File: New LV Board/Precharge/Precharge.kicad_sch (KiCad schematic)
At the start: 12 parts, among them J1 Conn_01x07, Q1 DMN3404L, U1 LM324, U2 Optocoupler

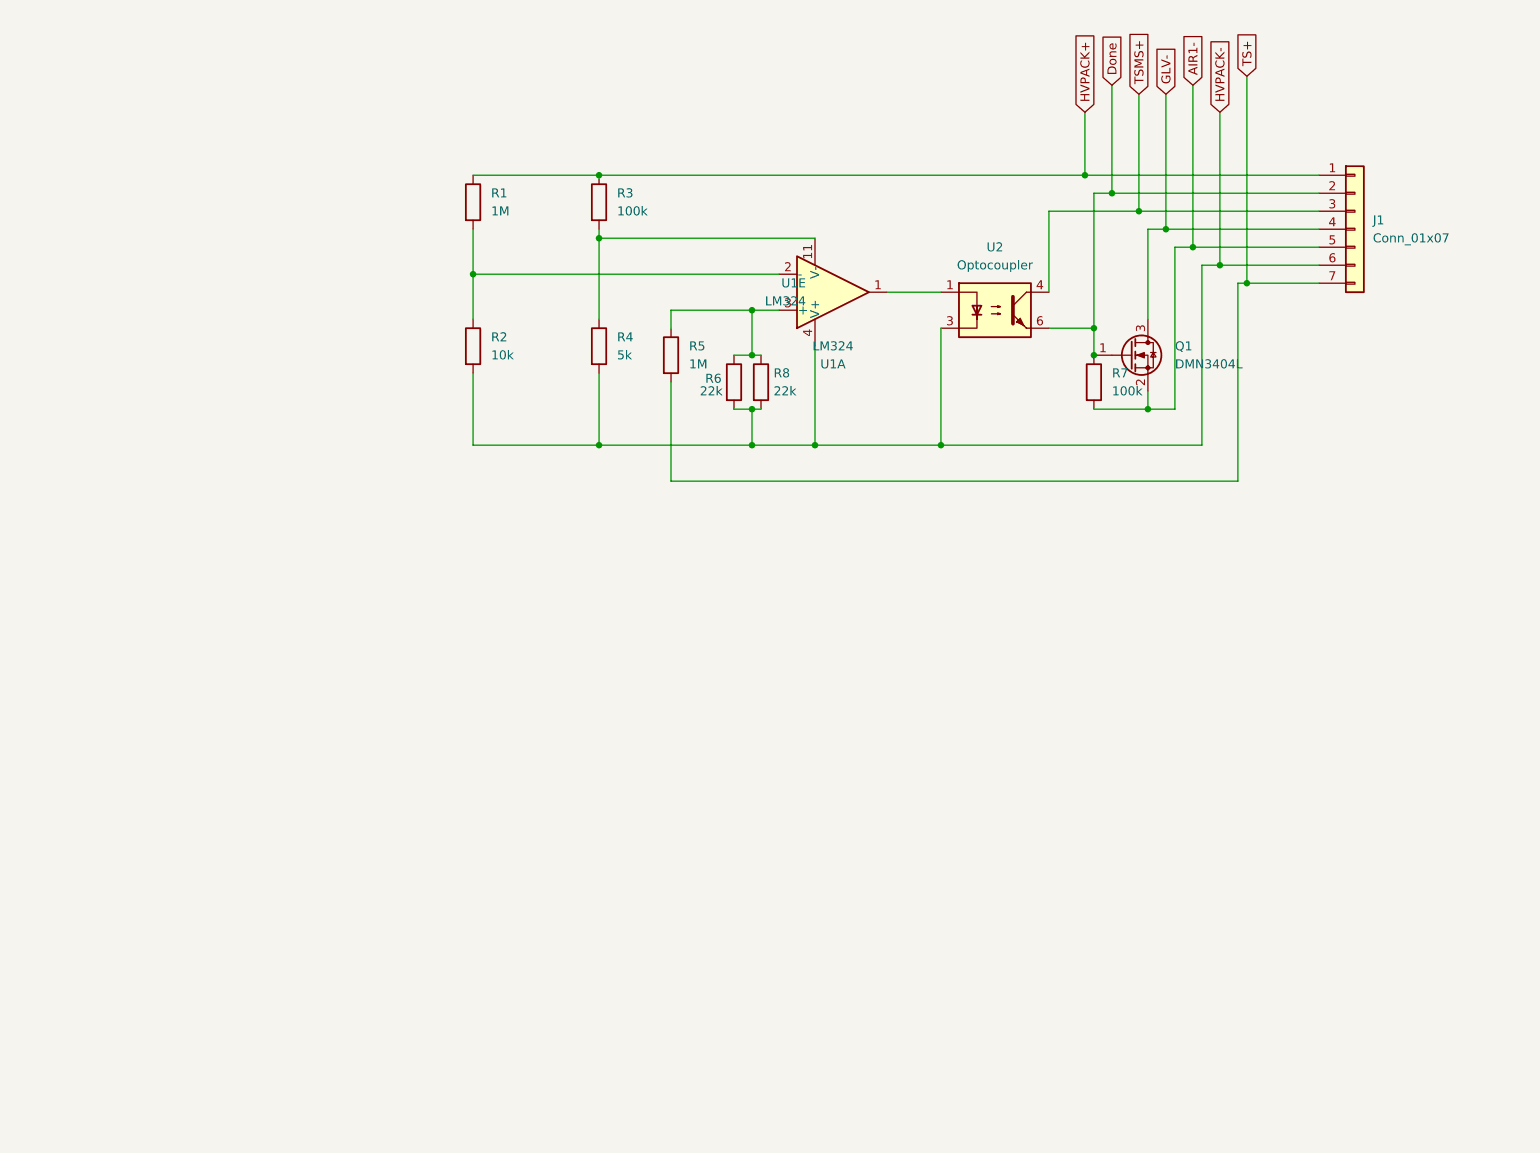
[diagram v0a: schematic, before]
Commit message: Update Precharge.kicad_sch
Added 555 Timer to Precharge design. PMOS Orientation makes it look ugly but it's chill. The 1ms that the pmos for the optocoupler is on will not effect it because during the first ms the opamp output is low.
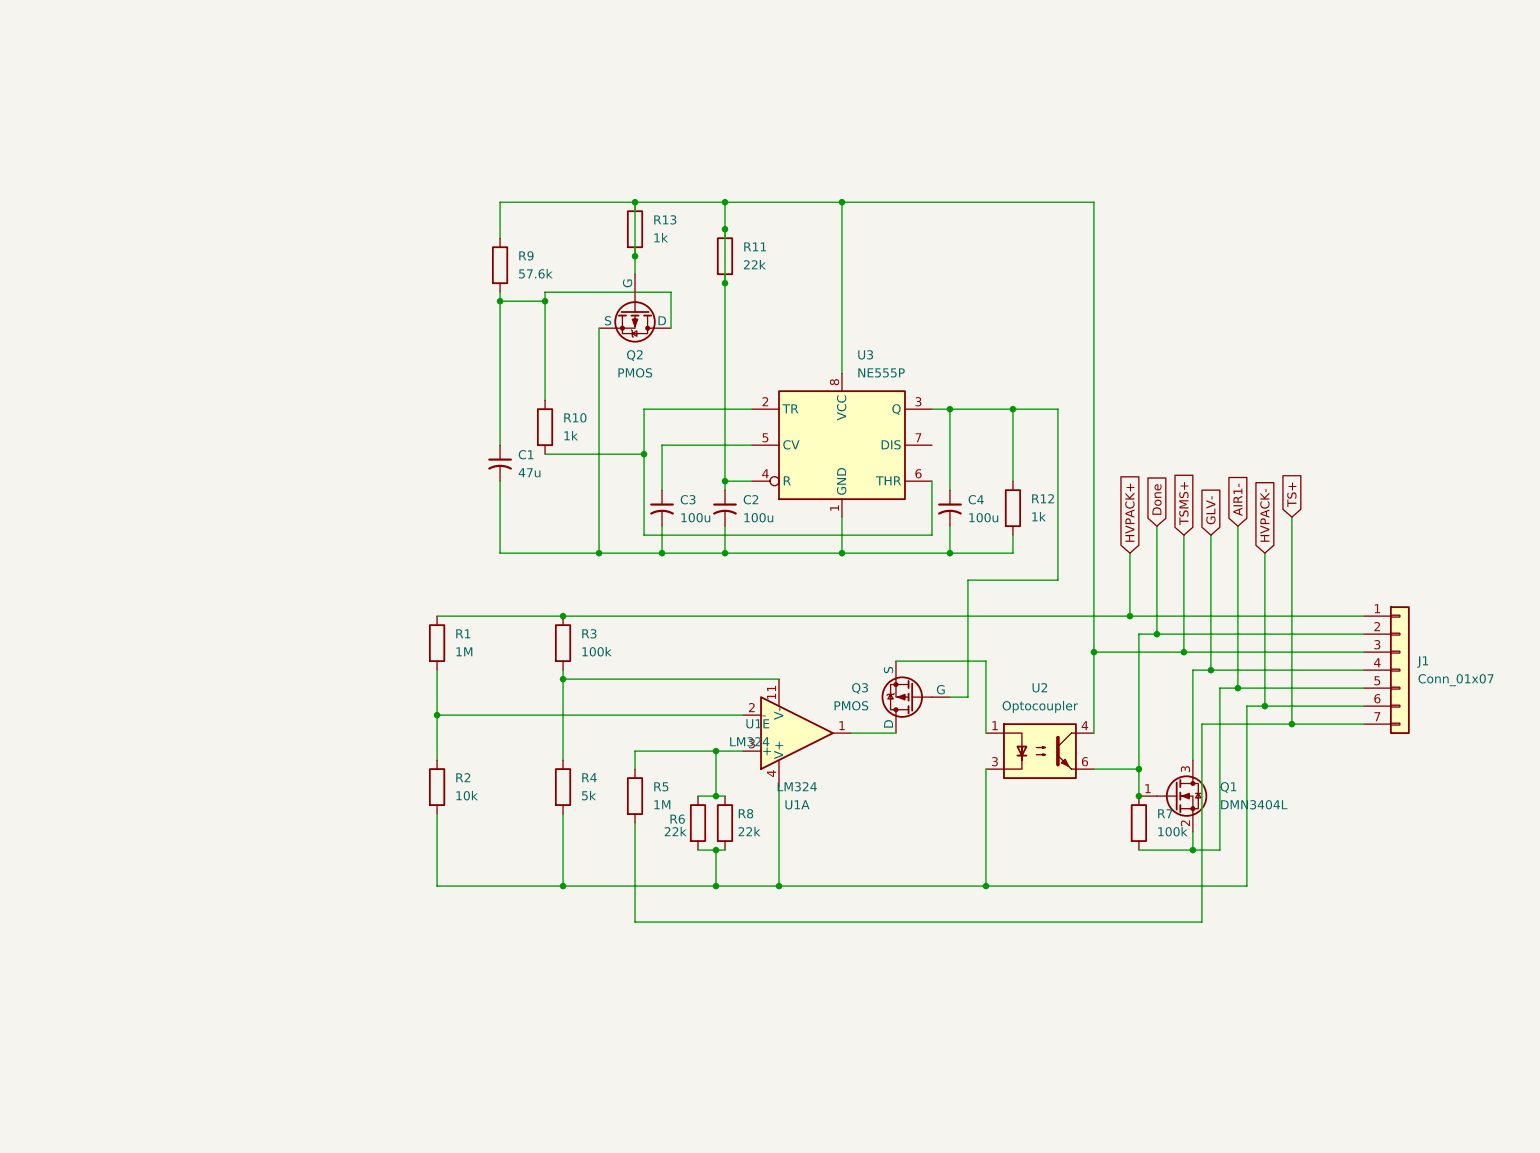
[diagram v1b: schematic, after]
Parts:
- added C1: 47u, symbol Device:C_Small_US
- added C2, C3, C4: 100u, symbol Device:C_Small_US
- added Q2, Q3: PMOS, symbol Simulation_SPICE:PMOS
- added R10, R12, R13: 1k, Resistor_THT:R_Axial_DIN0411_L9.9mm_D3.6mm_P7.62mm_Vertical, symbol Device:R
- added R11: 22k, Resistor_THT:R_Axial_DIN0411_L9.9mm_D3.6mm_P7.62mm_Vertical, symbol Device:R
- added R9: 57.6k, Resistor_THT:R_Axial_DIN0411_L9.9mm_D3.6mm_P7.62mm_Vertical, symbol Device:R
- added U3: NE555P, Package_DIP:DIP-8_W7.62mm, symbol Timer:NE555P
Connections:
- net TSMS+: now also C2.1, Q2.2 (G), R11.1, R11.2, R13.1, R13.2, R9.1, U3.4 (R), U3.8 (VCC)
- net at U1.1: now also Q3.1 (D); no longer U2.1
- new net: C4.1, Q3.2 (G), R12.1, U3.3 (Q)
- new net: Q3.3 (S), U2.1
- new net: C1.1, Q2.1 (D), R10.1, R9.2
- new net: R10.2, U3.2 (TR), U3.6 (THR)
- new net: C1.2, C2.2, C3.2, C4.2, Q2.3 (S), R12.2, U3.1 (GND)
- new net: C3.1, U3.5 (CV)
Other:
- moved on the sheet: J1, Q1, R1, R2, R3, R4, R5, R6, R7, R8, U1A, U1E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

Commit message: Added 555 timer to schematic
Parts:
- removed unit 1 of U1
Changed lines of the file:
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@@
-	)
-	(symbol
-		(lib_id "Amplifier_Operational:LM324")
-		(at 128.27 119.38 0)
-		(mirror x)
-		(unit 1)
-		(exclude_from_sim no)
-		(in_bom yes)
-		(on_board yes)
-		(dnp no)
-		(property "Reference" "U1"
-			(at 128.27 129.54 0)
-			(effects
-				(font
-					(size 1.27 1.27)
-				)
-			)
-		)
-		(property "Value" "LM324"
-			(at 128.27 127 0)
-			(effects
-				(font
-					(size 1.27 1.27)
-				)
-			)
-		)
-		(property "Footprint" "Package_DIP:CERDIP-14_W7.62mm_SideBrazed"
-			(at 127 121.92 0)
-			(effects
-				(font
-					(size 1.27 1.27)
-				)
-				(hide yes)
-			)
-		)
-		(property "Datasheet" "https://www.ti.com/general/docs/suppproductinfo.tsp?distId=10&gotoUrl=http%253A%252F%252Fwww.ti.com%252Flit%252Fgpn%252Flm224"
-			(at 129.54 124.46 0)
-			(effects
-				(font
-					(size 1.27 1.27)
-				)
-				(hide yes)
-			)
-		)
-		(property "Description" "Low-Power, Quad-Operational Amplifiers, DIP-14/SOIC-14/SSOP-14"
-			(at 128.27 119.38 0)
-			(effects
-				(font
-					(size 1.27 1.27)
-				)
-				(hide yes)
-			)
-		)
-		(pin "2"
-		)
-		(pin "3"
-		)
-		(pin "10"
-		)
-		(pin "7"
-		)
-		(pin "6"
-		)
-		(pin "9"
-		)
-		(pin "11"
-		)
-		(pin "14"
-		)
-		(pin "1"
-		)
-		(pin "12"
-		)
-		(pin "4"
-		)
-		(pin "5"
-		)
-		(pin "8"
-		)
-		(pin "13"
-		)
-		(instances
-			(project ""
-				(path "/99e1f855-54eb-435b-b064-69873828d7da"
-					(reference "U1")
-					(unit 1)
-				)
-			)
-		)
 	)
 	(symbol

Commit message: hi
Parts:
- C1, C2, C3, C4: footprint (none) -> Capacitor_SMD:C_1210_3225Metric_Pad1.33x2.70mm_HandSolder
- Q1: footprint Package_TO_SOT_SMD:SOT-23-3 -> Package_TO_SOT_THT:TO-220-3_Horizontal_TabDown
- Q2, Q3: footprint (none) -> Package_TO_SOT_THT:TO-220-3_Horizontal_TabDown
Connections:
- net GLV-: now also C1.2, C2.2, C3.2, C4.2, Q2.3 (S), R12.2, U3.1 (GND)
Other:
- moved on the sheet: Q3
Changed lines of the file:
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@@
 	)
 	(junction
+		(at 158.75 93.98)
+		(diameter 0)
+		(color 0 0 0 0)
+	)
+	(junction
 		(at 86.36 58.42)
 		(diameter 0)
@@
 	)
 	(junction
+		(at 184.15 110.49)
+		(diameter 0)
+		(color 0 0 0 0)
+	)
+	(junction
 		(at 118.11 48.26)
 		(diameter 0)
@@
 	(wire
 		(pts
-			(xy 154.94 119.38) (xy 154.94 109.22)
+			(xy 172.72 93.98) (xy 172.72 110.49)
+		)
+		(stroke
+			(width 0)
+			(type default)
+		)
+	)
+	(wire
+		(pts
+			(xy 154.94 109.22) (xy 154.94 119.38)
 		)
 		(stroke
@@
 	(wire
 		(pts
-			(xy 154.94 109.22) (xy 142.24 109.22)
+			(xy 158.75 93.98) (xy 172.72 93.98)
+		)
+		(stroke
+			(width 0)
+			(type default)
+		)
+	)
+	(wire
+		(pts
+			(xy 154.94 109.22) (xy 140.97 109.22)
 		)
 		(stroke
@@
 	(wire
 		(pts
+			(xy 172.72 110.49) (xy 184.15 110.49)
+		)
+		(stroke
+			(width 0)
+			(type default)
+		)
+	)
+	(wire
+		(pts
 			(xy 170.18 107.95) (xy 170.18 44.45)
 		)
@@
 	(wire
 		(pts
-			(xy 135.89 119.38) (xy 142.24 119.38)
+			(xy 135.89 119.38) (xy 140.97 119.38)
 		)
 		(stroke
@@
 	(wire
 		(pts
-			(xy 149.86 114.3) (xy 152.4 114.3)
+			(xy 148.59 114.3) (xy 152.4 114.3)
 		)
 		(stroke
@@
 			)
 		)
-		(property "Footprint" "Package_TO_SOT_SMD:SOT-23-3"
+		(property "Footprint" "Package_TO_SOT_THT:TO-220-3_Horizontal_TabDown"
 			(at 186.69 130.175 0)
 			(effects
@@
 			)
 		)
-		(property "Datasheet" "http://www.diodes.com/assets/Datasheets/ds31787.pdf"
+		(property "Datasheet" "IRF640NPBF"
 			(at 186.69 132.08 0)
 			(effects
@@
 	(symbol
 		(lib_id "Simulation_SPICE:PMOS")
-		(at 144.78 114.3 180)
+		(at 143.51 114.3 180)
 		(unit 1)
 		(exclude_from_sim no)
@@
 		(fields_autoplaced yes)
 		(property "Reference" "Q3"
-			(at 138.43 113.0299 0)
+			(at 137.16 113.0299 0)
 			(effects
 				(font
@@
 		)
 		(property "Value" "PMOS"
-			(at 138.43 115.5699 0)
+			(at 137.16 115.5699 0)
 			(effects
 				(font
@@
 			)
 		)
-		(property "Footprint" ""
-			(at 139.7 116.84 0)
+		(property "Footprint" "Package_TO_SOT_THT:TO-220-3_Horizontal_TabDown"
+			(at 138.43 116.84 0)
 			(effects
 				(font
@@
 			)
 		)
-		(property "Datasheet" "https://ngspice.sourceforge.io/docs/ngspice-html-manual/manual.xhtml#cha_MOSFETs"
-			(at 144.78 101.6 0)
+		(property "Datasheet" "IRF9Z34NPBF"
+			(at 143.51 101.6 0)
 			(effects
 				(font
@@
 		)
 		(property "Description" "P-MOSFET transistor, drain/source/gate"
-			(at 144.78 114.3 0)
+			(at 143.51 114.3 0)
 			(effects
 				(font
@@
 		)
 		(property "Sim.Device" "PMOS"
-			(at 144.78 97.155 0)
+			(at 143.51 97.155 0)
 			(effects
 				(font
@@
 		)
 		(property "Sim.Type" "VDMOS"
-			(at 144.78 95.25 0)
+			(at 143.51 95.25 0)
 			(effects
 				(font
@@
 		)
 		(property "Sim.Pins" "1=D 2=G 3=S"
-			(at 144.78 99.06 0)
+			(at 143.51 99.06 0)
 			(effects
 				(font
@@
 			)
 		)
-		(property "Footprint" ""
+		(property "Footprint" "Capacitor_SMD:C_1210_3225Metric_Pad1.33x2.70mm_HandSolder"
 			(at 149.86 87.63 0)
 			(effects
@@
 			)
 		)
-		(property "Footprint" ""
+		(property "Footprint" "Package_TO_SOT_THT:TO-220-3_Horizontal_TabDown"
 			(at 107.95 64.77 0)
 			(effects
@@
 			)
 		)
-		(property "Datasheet" "https://ngspice.sourceforge.io/docs/ngspice-html-manual/manual.xhtml#cha_MOSFETs"
+		(property "Datasheet" "IRF9Z34NPBF"
 			(at 92.71 59.69 0)
 			(effects
@@
 			)
 		)
-		(property "Footprint" ""
+		(property "Footprint" "Capacitor_SMD:C_1210_3225Metric_Pad1.33x2.70mm_HandSolder"
 			(at 86.36 81.28 0)
 			(effects
@@
 			)
 		)
-		(property "Footprint" ""
+		(property "Footprint" "Capacitor_SMD:C_1210_3225Metric_Pad1.33x2.70mm_HandSolder"
 			(at 109.22 87.63 0)
 			(effects
@@
 			)
 		)
-		(property "Footprint" ""
+		(property "Footprint" "Capacitor_SMD:C_1210_3225Metric_Pad1.33x2.70mm_HandSolder"
 			(at 118.11 87.63 0)
 			(effects

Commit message: precharge
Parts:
- removed C2, C4: 100u, Capacitor_SMD:C_1210_3225Metric_Pad1.33x2.70mm_HandSolder, symbol Device:C_Small_US
- removed J1: Conn_01x07, Connector_JST:JST_EH_B7B-EH-A_1x07_P2.50mm_Vertical, symbol Connector_Generic:Conn_01x07
- removed Q1: DMN3404L, Package_TO_SOT_THT:TO-220-3_Horizontal_TabDown, symbol Transistor_FET:DMN3404L
- removed Q2, Q3: PMOS, Package_TO_SOT_THT:TO-220-3_Horizontal_TabDown, symbol Simulation_SPICE:PMOS
- removed R11: 22k, Resistor_THT:R_Axial_DIN0411_L9.9mm_D3.6mm_P7.62mm_Vertical, symbol Device:R
- removed R12, R13: 1k, Resistor_THT:R_Axial_DIN0411_L9.9mm_D3.6mm_P7.62mm_Vertical, symbol Device:R
- removed U1: LM324, Package_DIP:CERDIP-14_W7.62mm_SideBrazed, symbol Amplifier_Operational:LM324
- added C5, C7: 0.1u, symbol Device:C
- added C6: 1u, symbol Device:C
- added Q1: BSS214NW, Package_TO_SOT_SMD:SOT-323_SC-70_Handsoldering, symbol Transistor_FET:BSS214NW
- added Q2: MPSA42, Package_TO_SOT_THT:TO-92, symbol Transistor_BJT:MPSA42
- added Q4: IRLML5203, Package_TO_SOT_SMD:SOT-23_Handsoldering, symbol Transistor_FET:IRLML5203
- added R14: 2k, Resistor_THT:R_Axial_DIN0411_L9.9mm_D3.6mm_P7.62mm_Vertical, symbol Device:R
- added R15: 2.2k, Resistor_THT:R_Axial_DIN0411_L9.9mm_D3.6mm_P7.62mm_Vertical, symbol Device:R
- added R16: 22k, Resistor_THT:R_Axial_DIN0411_L9.9mm_D3.6mm_P7.62mm_Vertical, symbol Device:R
- added R17: 220, Resistor_THT:R_Axial_DIN0411_L9.9mm_D3.6mm_P7.62mm_Vertical, symbol Device:R
- added R18, R19: 100k, Resistor_THT:R_Axial_DIN0411_L9.9mm_D3.6mm_P7.62mm_Vertical, symbol Device:R
- added U1: LM2903, Package_DIP:DIP-8_W7.62mm, symbol Comparator:LM2903
- added U4: LR8N3-G, Package_TO_SOT_THT:TO-92, symbol Regulator_Linear:LR8N3-G
- C3: value 100u -> 0.1u
- R1, R5: value 1M -> 100k
- R10: value 1k -> 10k
- R2: value 10k -> 100k
- R3: value 100k -> 2k
- R4: value 5k -> 22k
- R6: value 22k -> 100k
- R7: Wattage (none) -> 2
- R8: value 22k -> 100k; Watt (none) -> 2
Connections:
- net AIR1-: now also Q1.3 (D); no longer R7.2
- net Done: now also R10.1, Q1.1 (G); no longer R7.1
- net GLV-: now also R10.2, Q1.2 (S); no longer C1.2, C3.2, U3.1 (GND)
- net HVPACK+: now also R18.1, R19.1; no longer R3.1
- net HVPACK-: now also R3.2, C5.2, C7.2, R14.2, R16.2, U1.4 (V-); no longer R2.2, R4.2, R8.2
- net TS+: now also R7.1; no longer R5.2
- net TSMS+: now also Q2.2 (B), Q4.2 (S); no longer U2.4
- net at U3.3 (Q): now also Q4.1 (G)
- net at U2.1: now also U1.1
- net at C1.1, R9.2: now also U3.2 (TR), U3.6 (THR), Q2.3 (C); no longer R10.1
- net at R4.1: now also R2.2, R3.1; no longer R3.2
- net at U3.7 (DIS): now also Q2.1 (E)
- new net: R4.2, R5.1, U1.3 (+)
- new net: C6.1, R18.2, R19.2, U4.1 (IN)
- new net: C6.2, R15.2, R16.1, R17.2, U4.3 (ADJ)
- new net: C5.1, C7.1, R15.1, R17.1, U1.8 (V+), U4.2 (OUT)
- new net: Q4.3 (D), U2.4
- new net: R14.1, R8.2, U1.2 (-)
- new net: C1.2, C3.2, U3.1 (GND)
- new net: R7.2, R8.1
- new net: R5.2, R6.1
- no-connect marks 0 -> 3
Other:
- moved on the sheet: C1, C3, R1, R2, R9, U2, U3

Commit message: Precharge work
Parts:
- removed R1, R18, R19, R2, R7, R8: 100k, Resistor_THT:R_Axial_DIN0411_L9.9mm_D3.6mm_P7.62mm_Vertical, symbol Device:R
- removed R17: 220, Resistor_THT:R_Axial_DIN0411_L9.9mm_D3.6mm_P7.62mm_Vertical, symbol Device:R
- removed U1: LM2903, Package_DIP:DIP-8_W7.62mm, symbol Comparator:LM2903
- removed U2: Optocoupler, Package_SO:SOIC-4_4.55x3.7mm_P2.54mm, symbol Isolator:Optocoupler_DC_PhotoNPN_AKEC
- added K1: G3VM-61G2, Precharge:G-SOP4_OMR, symbol Precharge:G3VM-61G2
- added R1, R11, R12, R2, R7, R8: 100k, Resistor_THT:R_Axial_DIN0516_L15.5mm_D5.0mm_P5.08mm_Vertical, symbol Device:R_US
- added R13: 2k, Resistor_THT:R_Axial_DIN0207_L6.3mm_D2.5mm_P2.54mm_Vertical, symbol Device:R
- added U1: LM2904, Package_DIP:DIP-8_W7.62mm, symbol Amplifier_Operational:LM2904
- C1: Link (none) -> https://www.digikey.com/en/products/detail/samsung-electro-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; Name (none) -> 47u Cap
- C3: footprint Capacitor_SMD:C_1210_3225Metric_Pad1.33x2.70mm_HandSolder -> Capacitor_SMD:C_1206_3216Metric_Pad1.33x1.80mm_HandSolder; Link (none) -> https://www.digikey.com/en/products/detail/samsung-electro-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; Name (none) -> 0.1u Cap
- C5, C7: footprint (none) -> Capacitor_SMD:C_1206_3216Metric_Pad1.33x1.80mm_HandSolder; Link (none) -> https://www.digikey.com/en/products/detail/samsung-electro-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; Name (none) -> 0.1u Cap
- C6: footprint (none) -> Capacitor_SMD:C_1206_3216Metric_Pad1.33x1.80mm_HandSolder; Link (none) -> https://www.digikey.com/en/products/detail/samsung-electro-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; Name (none) -> 1u Cap
- Q1: Link (none) -> https://www.digikey.at/en/products/detail/infineon-technolo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; Name (none) -> NMOS
- Q2: Link (none) -> https://www.digikey.com/en/products/detail/onsemi/MPSA42/32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; Name (none) -> PNP Transistor
- Q4: Link (none) -> https://www.digikey.com/en/products/detail/infineon-technol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; Name (none) -> PMOS
- R10: footprint Resistor_THT:R_Axial_DIN0411_L9.9mm_D3.6mm_P7.62mm_Vertical -> Resistor_THT:R_Axial_DIN0207_L6.3mm_D2.5mm_P2.54mm_Vertical; Name (none) -> 10k Resistor
- R14: value 2k -> 22k; footprint Resistor_THT:R_Axial_DIN0411_L9.9mm_D3.6mm_P7.62mm_Vertical -> Resistor_THT:R_Axial_DIN0207_L6.3mm_D2.5mm_P2.54mm_Vertical; Name (none) -> 22k Resistor
- R15: footprint Resistor_THT:R_Axial_DIN0411_L9.9mm_D3.6mm_P7.62mm_Vertical -> Resistor_THT:R_Axial_DIN0207_L6.3mm_D2.5mm_P2.54mm_Vertical; Name (none) -> 2.2k Resistor
- R16: value 22k -> 220; footprint Resistor_THT:R_Axial_DIN0411_L9.9mm_D3.6mm_P7.62mm_Vertical -> Resistor_THT:R_Axial_DIN0207_L6.3mm_D2.5mm_P2.54mm_Vertical; Name (none) -> 220 Resistor
- R3: footprint Resistor_THT:R_Axial_DIN0411_L9.9mm_D3.6mm_P7.62mm_Vertical -> Resistor_THT:R_Axial_DIN0207_L6.3mm_D2.5mm_P2.54mm_Vertical; Name (none) -> 2k Resistor
- R4: footprint Resistor_THT:R_Axial_DIN0411_L9.9mm_D3.6mm_P7.62mm_Vertical -> Resistor_THT:R_Axial_DIN0207_L6.3mm_D2.5mm_P2.54mm_Vertical; Name (none) -> 22k Resistor
- R5, R6: footprint Resistor_THT:R_Axial_DIN0411_L9.9mm_D3.6mm_P7.62mm_Vertical -> Resistor_THT:R_Axial_DIN0207_L6.3mm_D2.5mm_P2.54mm_Vertical; Name (none) -> 100k Resistor
- R9: footprint Resistor_THT:R_Axial_DIN0411_L9.9mm_D3.6mm_P7.62mm_Vertical -> Resistor_THT:R_Axial_DIN0207_L6.3mm_D2.5mm_P2.54mm_Vertical; Name (none) -> 57.6k Resistor
- U3: Link (none) -> https://www.digikey.com/en/products/detail/texas-instrument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; Name (none) -> 555 Timer
- U4: Link (none) -> https://www.digikey.com/en/products/detail/microchip-techno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; Name (none) -> Linear Voltage Regulator
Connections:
- net Done: now also K1.3
- net GLV-: now also C1.2, C3.2, U3.1 (GND)
- net HVPACK+: now also R11.1, R12.1, R2.1
- net HVPACK-: now also K1.2, R13.2, U1.4 (V-); no longer R16.2
- net TS+: now also R8.1
- net at R3.1, R4.1: now also R1.2
- net at R4.2, R5.1: now also U1.3 (+)
- net at C6.1, U4.1 (IN): now also C6.2, R14.1, R15.2, R16.2, U4.3 (ADJ), R11.2, R12.2
- net at C5.1, C7.1, R15.1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: now also R16.1, U1.8 (V+)
- net at Q4.3 (D): now also K1.4
- new net: K1.1, U1.1
- new net: R1.1, R2.2
- new net: R13.1, R7.2, U1.2 (-)
- new net: R7.1, R8.2
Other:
- moved on the sheet: C1, C3, C5, C7, Q1, Q2, Q4, R10, R15, R3, R4, R6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

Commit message: schemati
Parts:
- removed C5: 0.1u, Capacitor_SMD:C_1206_3216Metric_Pad1.33x1.80mm_HandSolder, symbol Device:C
- R11, R12: footprint Resistor_THT:R_Axial_DIN0516_L15.5mm_D5.0mm_P5.08mm_Vertical -> Resistor_THT:R_Axial_DIN0516_L15.5mm_D5.0mm_P7.62mm_Vertical
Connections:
- net at C6.2, R14.1, R15.2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: no longer C6.1, R11.2, R12.2, U4.1 (IN)
- new net: C6.1, R11.2, R12.2, U4.1 (IN)
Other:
- moved on the sheet: C6, C7, R1, R11, R12, R13, R14, R15, R16, R2, R3, R4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
